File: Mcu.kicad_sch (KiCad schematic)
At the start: 27 parts, among them J8 AUX0, J9 AUX0, U7 STM32H723VGHx, X2 X322516MLB4SI

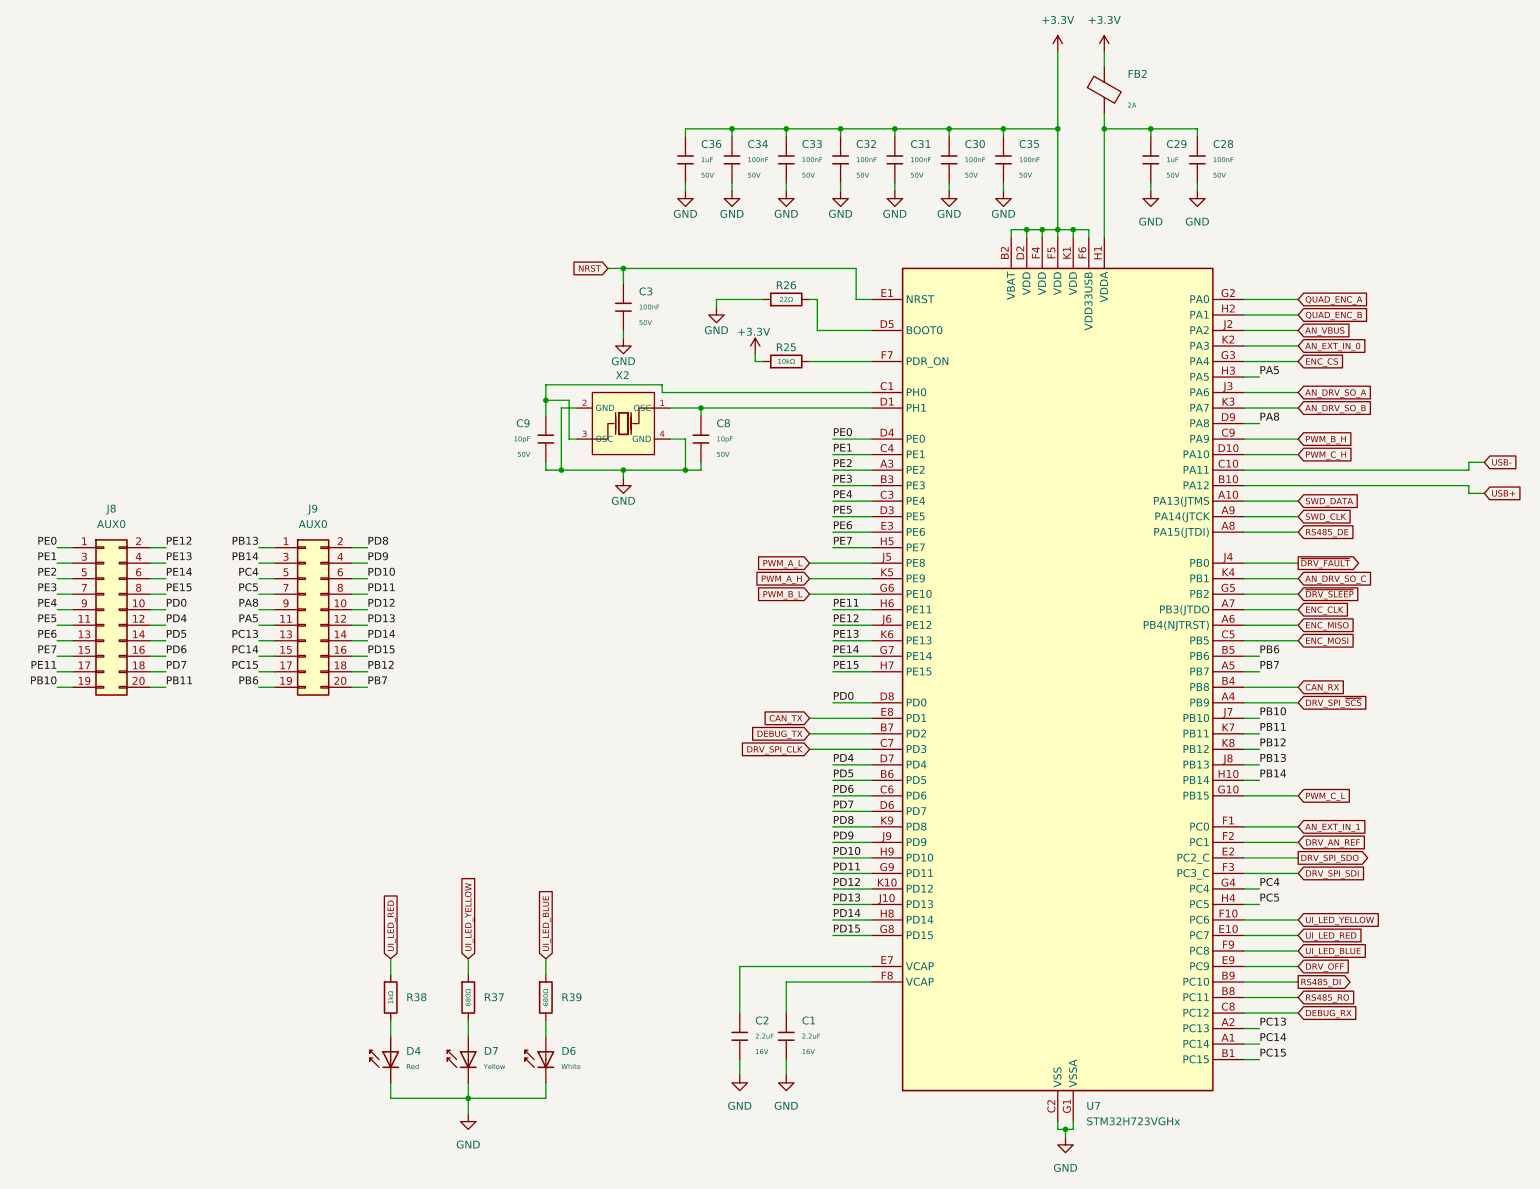
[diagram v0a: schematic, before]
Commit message: Reroute mcu lines, updated can, motor timer pins
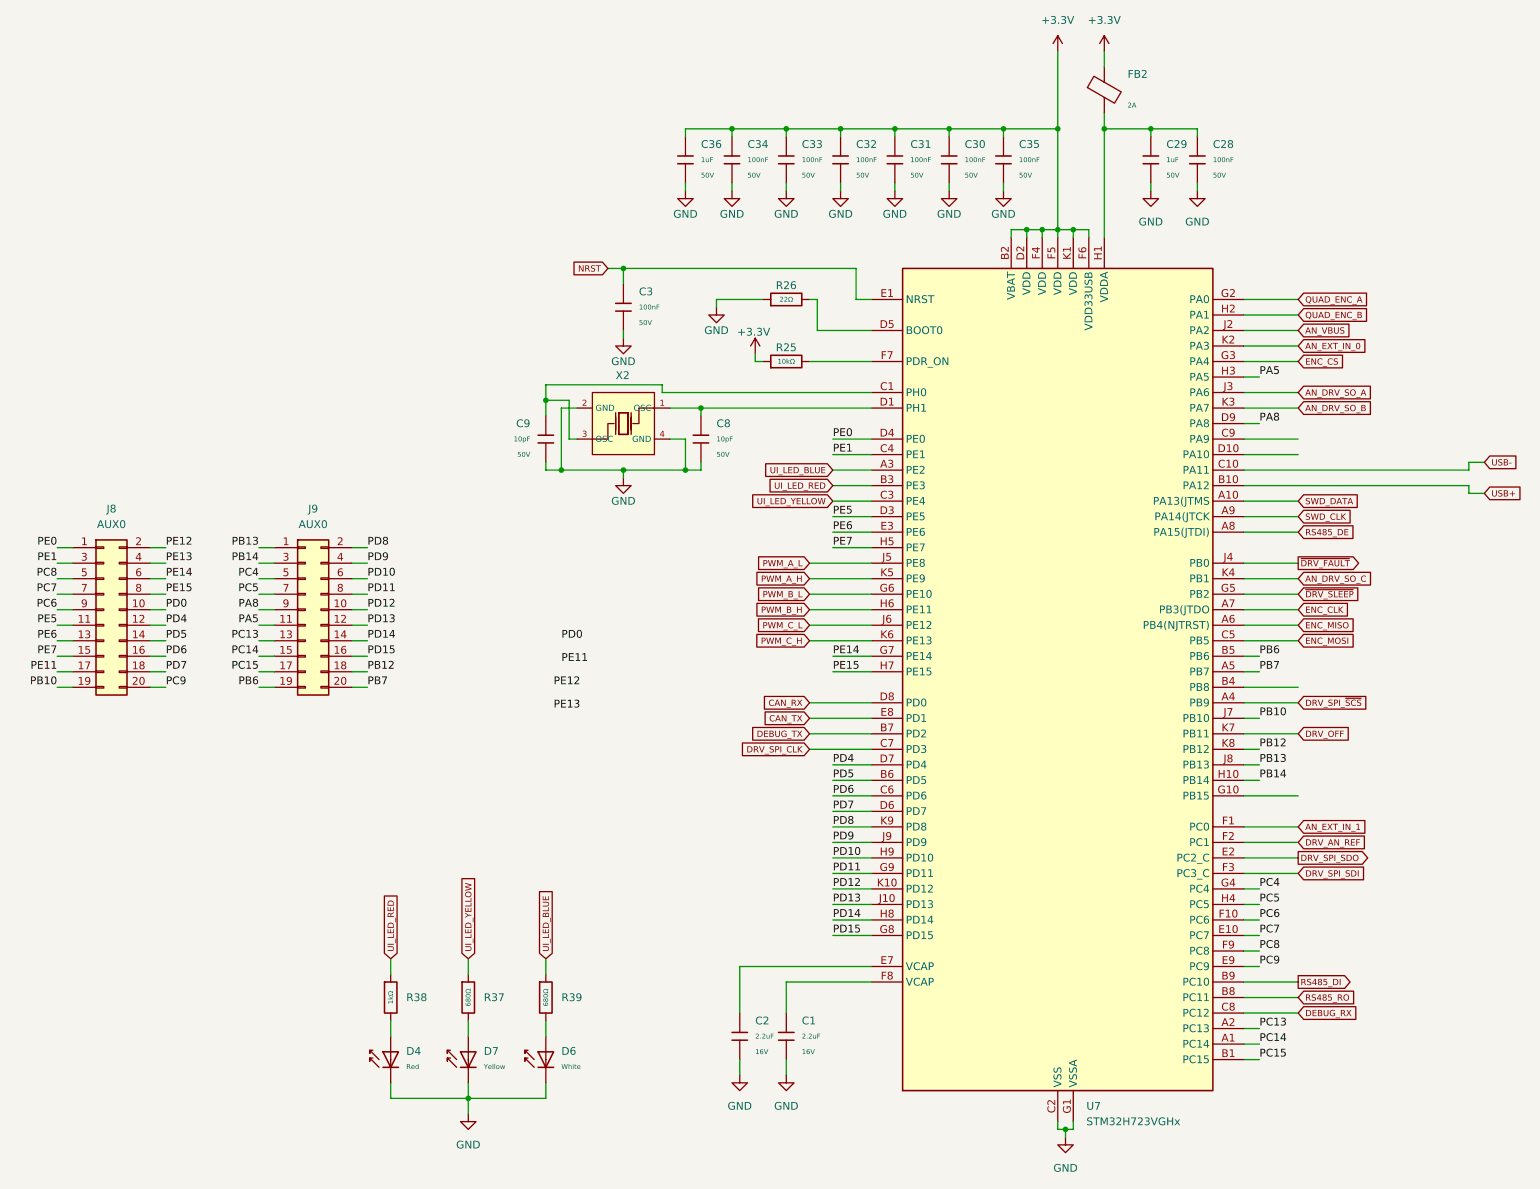
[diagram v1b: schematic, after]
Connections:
- net CAN_RX: now also U7.D8 (PD0); no longer U7.B4 (PB8)
- net DRV_OFF: now also U7.K7 (PB11); no longer U7.E9 (PC9)
- net PD0: no longer U7.D8 (PD0)
- net PE11: no longer U7.H6 (PE11)
- net PE12: no longer U7.J6 (PE12)
- net PE13: no longer U7.K6 (PE13)
- net PWM_B_H: now also U7.H6 (PE11); no longer U7.C9 (PA9)
- net PWM_C_H: now also U7.K6 (PE13); no longer U7.D10 (PA10)
- net PWM_C_L: now also U7.J6 (PE12); no longer U7.G10 (PB15)
- net UI_LED_BLUE: now also U7.A3 (PE2); no longer U7.F9 (PC8)
- net UI_LED_RED: now also U7.B3 (PE3); no longer U7.E10 (PC7)
- net UI_LED_YELLOW: now also U7.C3 (PE4); no longer U7.F10 (PC6)
- net PB11 renamed PC9
- net PC9: now also U7.E9 (PC9); no longer U7.K7 (PB11)
- net PE2 renamed PC8
- net PC8: now also U7.F9 (PC8); no longer U7.A3 (PE2)
- net PE3 renamed PC7
- net PC7: now also U7.E10 (PC7); no longer U7.B3 (PE3)
- net PE4 renamed PC6
- net PC6: now also U7.F10 (PC6); no longer U7.C3 (PE4)

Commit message: Finished layout, pcba is being tested
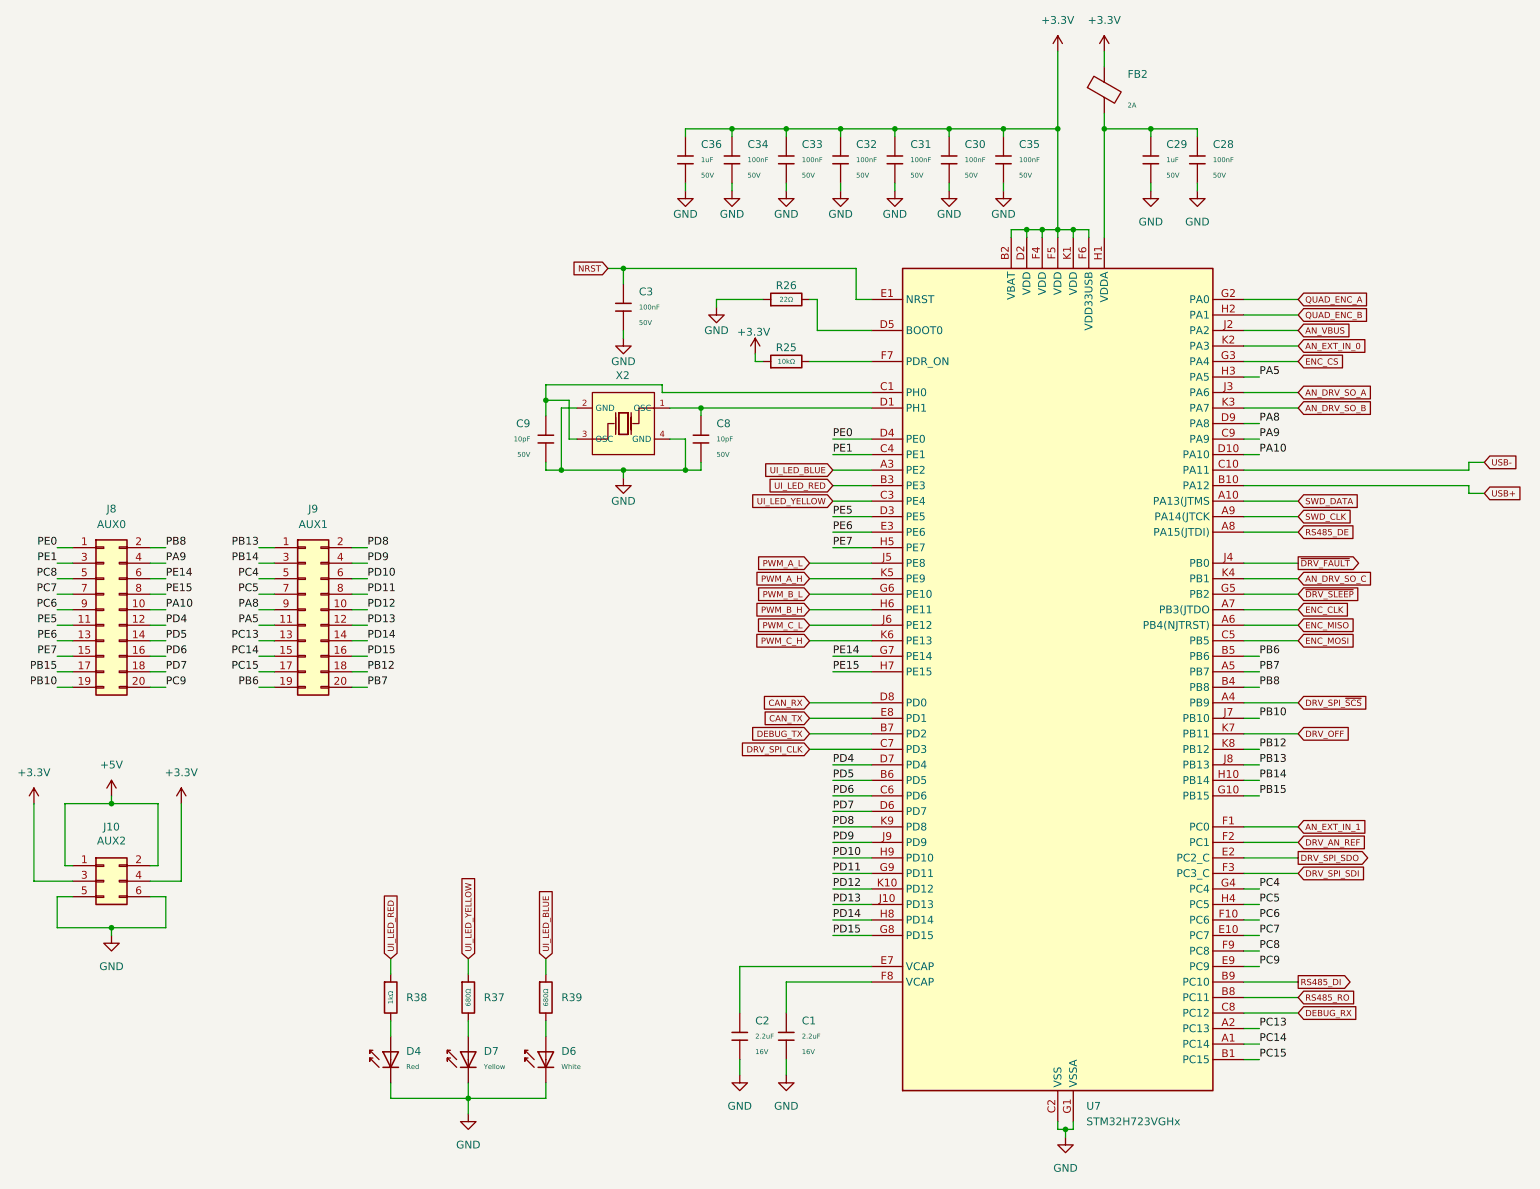
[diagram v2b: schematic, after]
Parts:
- added J10: AUX2, Connector_PinSocket_2.54mm:PinSocket_2x03_P2.54mm_Vertical, symbol Connector_Generic:Conn_02x03_Odd_Even
- J9: value AUX0 -> AUX1
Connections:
- net PD0 is gone; now on net PA10: J8.10 (Pin_10)
- net PE11 is gone; now on net PB15: J8.17 (Pin_17)
- net PE12 is gone; now on net PB8: J8.2 (Pin_2)
- net PE13 is gone; now on net PA9: J8.4 (Pin_4)
- net +3.3V: now also J10.3 (Pin_3), J10.4 (Pin_4)
- net GND: now also J10.5 (Pin_5), J10.6 (Pin_6)
- net PB8: now reaches U7.B4 (PB8)
- net PA9: now reaches U7.C9 (PA9)
- net PA10: now reaches U7.D10 (PA10)
- net PB15: now reaches U7.G10 (PB15)
- new net +5V: J10.1 (Pin_1), J10.2 (Pin_2)
